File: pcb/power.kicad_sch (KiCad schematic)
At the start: 20 parts, among them U10 NCP163AFCT120T2G, U4 NCP163AFCT330T2G, U5 TPS82695, U9 NCP163AFCT180T2G

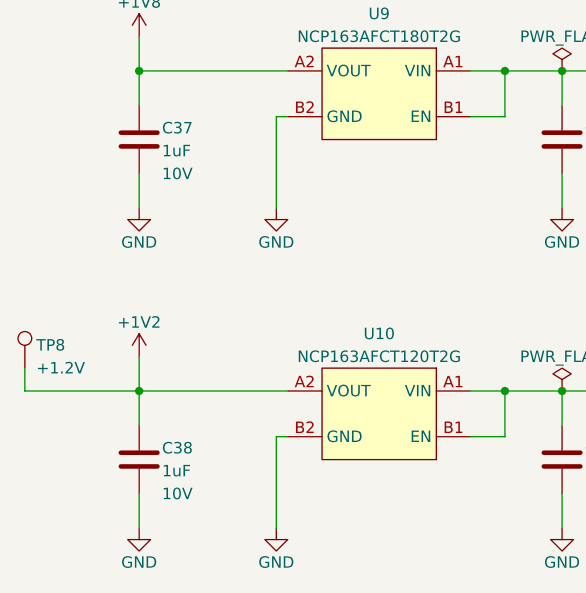
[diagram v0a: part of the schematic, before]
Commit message: Rev. A initial design prior to fab comments
- BOM simplification
- Added my initials to the board
- Made the board more easy to panlize
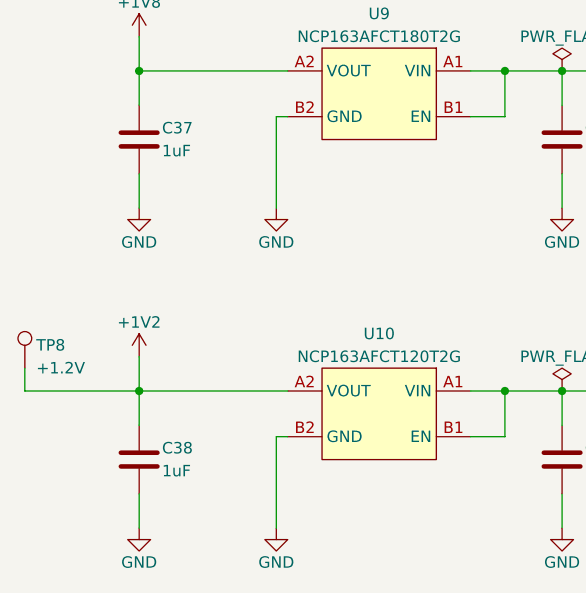
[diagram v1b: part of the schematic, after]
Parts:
- C37, C38: Voltage 10V -> (none)
- TP4, TP8: now left out of the parts list
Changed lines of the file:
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@@
   )
   (symbol (lib_id "Connector:TestPoint") (at 52.07 153.67 0) (unit 1)
-    (in_bom yes) (on_board yes)
+    (in_bom no) (on_board yes)
     (property "Reference" "TP8" (id 0) (at 53.34 151.13 0)
       (effects (font (size 1.27 1.27)) (justify left))
@@
   )
   (symbol (lib_id "Connector:TestPoint") (at 52.07 41.91 0) (unit 1)
-    (in_bom yes) (on_board yes)
+    (in_bom no) (on_board yes)
     (property "Reference" "TP4" (id 0) (at 53.34 39.37 0)
       (effects (font (size 1.27 1.27)) (justify left))
@@
     (property "Datasheet" "~" (id 3) (at 64.77 163.83 0)
       (effects (font (size 1.27 1.27)) hide)
-    )
-    (property "Voltage" "10V" (id 4) (at 67.31 167.64 0)
-      (effects (font (size 1.27 1.27)) (justify left))
     )
     (pin "1")
@@
       (effects (font (size 1.27 1.27)) hide)
     )
-    (property "Voltage" "10V" (id 4) (at 67.31 132.08 0)
-      (effects (font (size 1.27 1.27)) (justify left))
-    )
-    (pin "1")
+    (pin "1")

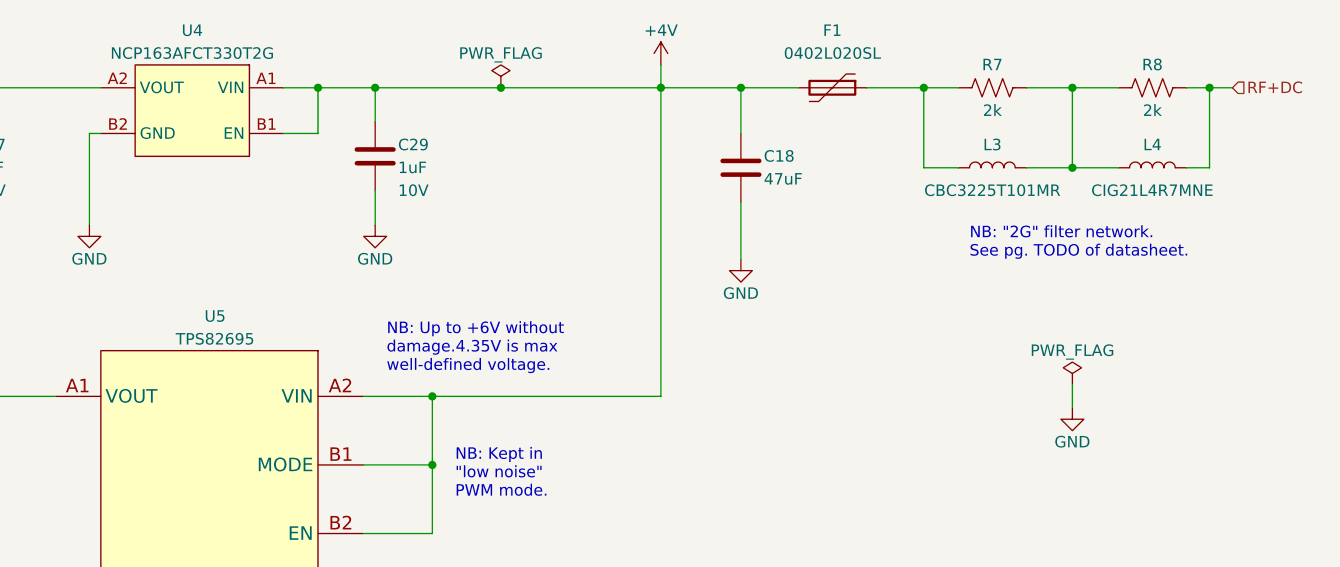
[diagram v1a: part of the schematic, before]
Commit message: Small changes before speedy fabrication
- This is revision A
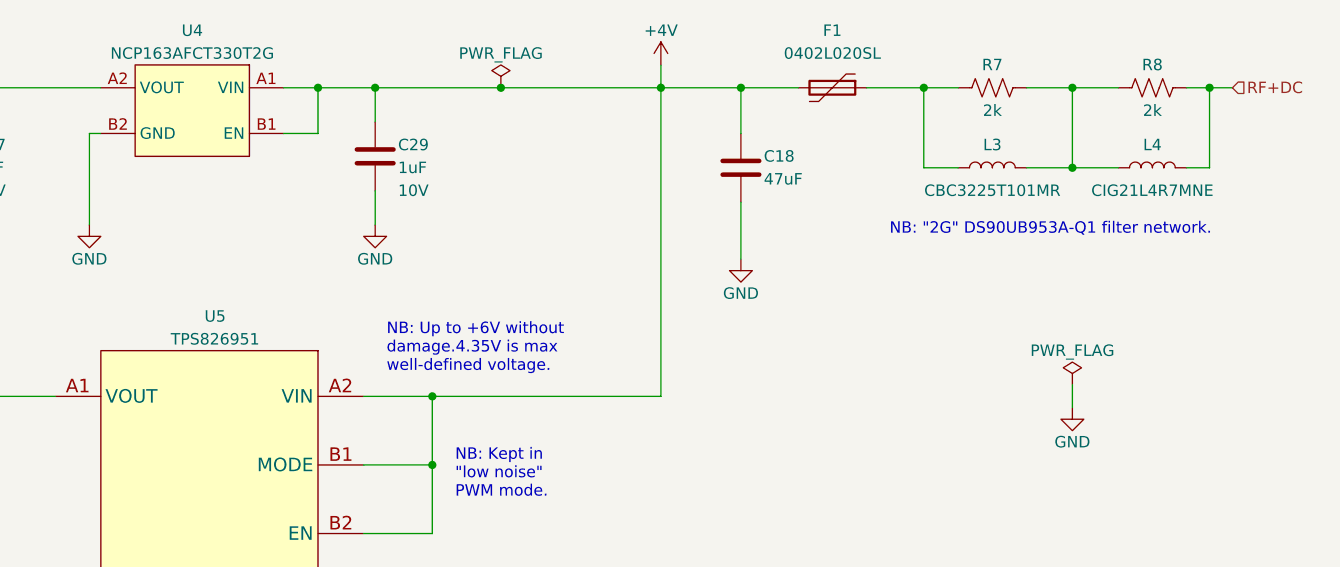
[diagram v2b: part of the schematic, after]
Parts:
- U5: value TPS82695 -> TPS826951
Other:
- note added: "NB: "2G" DS90UB953A-Q1 filter network."
- note removed: "NB: "2G" filter network. See pg. TODO of datasheet."
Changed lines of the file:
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@@
     (effects (font (size 1.27 1.27)) (justify left bottom))
   )
-  (text "NB: \"2G\" filter network.\nSee pg. TODO of datasheet."
-    (at 177.8 63.5 0)
+  (text "NB: \"2G\" DS90UB953A-Q1 filter network." (at 168.91 60.96 0)
     (effects (font (size 1.27 1.27)) (justify left bottom))
   )
@@
     (in_bom yes) (on_board yes)
     (property "Reference" "U5" (id 0) (at 93.98 69.85 0))
-    (property "Value" "TPS82695" (id 1) (at 93.98 72.39 0))
+    (property "Value" "TPS826951" (id 1) (at 93.98 72.39 0))
     (property "Footprint" "jonnew:TI_SIP0008B" (id 2) (at 93.98 109.22 0)
       (effects (font (size 1.27 1.27)) hide)

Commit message: Start of revision B
- Address the following issues
1. The photodiode anode is on pin 3, not pin 2
2. No paste on coax connector
3. CRESET_B needs to come out to programming header
4. Need PU on CS line.
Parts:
- C18, C37, C38: TempCo (none) -> X5R; Voltage (none) -> 10V
- C27, C29, C40, C41: TempCo (none) -> X5R
- TP4, TP8: DNP (none) -> DNP
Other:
- title: Headstage-RHS2116 -> Headstage-64s
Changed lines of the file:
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@@
   (paper "A4")
   (title_block
-    (title "Headstage-RHS2116")
+    (title "Headstage-64s")
     (date "2021-12-16")
-    (rev "A")
+    (rev "B")
     (company "Open Ephys, Inc")
     (comment 1 "Jonathan P. Newman")
@@
       (effects (font (size 1.27 1.27)) hide)
     )
+    (property "DNP" "DNP" (id 4) (at 52.07 153.67 0)
+      (effects (font (size 1.27 1.27)) hide)
+    )
     (pin "1")
   )
@@
       (effects (font (size 1.27 1.27)) hide)
     )
+    (property "DNP" "DNP" (id 4) (at 52.07 41.91 0)
+      (effects (font (size 1.27 1.27)) hide)
+    )
     (pin "1")
   )
@@
       (effects (font (size 1.27 1.27)) (justify left))
     )
+    (property "TempCo" "X5R" (id 5) (at 111.76 52.07 0)
+      (effects (font (size 1.27 1.27)) hide)
+    )
     (pin "1")
     (pin "2")
@@
     )
     (property "Datasheet" "~" (id 3) (at 64.77 163.83 0)
+      (effects (font (size 1.27 1.27)) hide)
+    )
+    (property "TempCo" "X5R" (id 4) (at 64.77 163.83 0)
+      (effects (font (size 1.27 1.27)) hide)
+    )
+    (property "Voltage" "10V" (id 5) (at 64.77 163.83 0)
       (effects (font (size 1.27 1.27)) hide)
     )
@@
     )
     (property "Datasheet" "~" (id 3) (at 152.4 53.34 0)
+      (effects (font (size 1.27 1.27)) hide)
+    )
+    (property "TempCo" "X5R" (id 4) (at 152.4 53.34 0)
+      (effects (font (size 1.27 1.27)) hide)
+    )
+    (property "Voltage" "10V" (id 5) (at 152.4 53.34 0)
       (effects (font (size 1.27 1.27)) hide)
     )
@@
       (effects (font (size 1.27 1.27)) hide)
     )
-    (property "Datasheet" "" (id 3) (at 91.44 46.99 0)
+    (property "Datasheet" "~" (id 3) (at 91.44 46.99 0)
       (effects (font (size 1.27 1.27)) hide)
     )
@@
     (property "Voltage" "10V" (id 4) (at 114.3 167.64 0)
       (effects (font (size 1.27 1.27)) (justify left))
+    )
+    (property "TempCo" "X5R" (id 5) (at 111.76 163.83 0)
+      (effects (font (size 1.27 1.27)) hide)
     )
     (pin "1")
@@
       (effects (font (size 1.27 1.27)) (justify left))
     )
+    (property "TempCo" "X5R" (id 5) (at 111.76 128.27 0)
+      (effects (font (size 1.27 1.27)) hide)
+    )
     (pin "1")
     (pin "2")
@@
       (effects (font (size 1.27 1.27)) (justify left))
     )
+    (property "TempCo" "X5R" (id 5) (at 64.77 52.07 0)
+      (effects (font (size 1.27 1.27)) hide)
+    )
     (pin "1")
     (pin "2")
@@
       (effects (font (size 1.27 1.27)) hide)
     )
+    (property "TempCo" "X5R" (id 4) (at 64.77 128.27 0)
+      (effects (font (size 1.27 1.27)) hide)
+    )
+    (property "Voltage" "10V" (id 5) (at 64.77 128.27 0)
+      (effects (font (size 1.27 1.27)) hide)
+    )
     (pin "1")
     (pin "2")
@@
       (effects (font (size 1.27 1.27)) hide)
     )
-    (property "Datasheet" "" (id 3) (at 91.44 158.75 0)
+    (property "Datasheet" "~" (id 3) (at 91.44 158.75 0)
       (effects (font (size 1.27 1.27)) hide)
     )
@@
       (effects (font (size 1.27 1.27)) hide)
     )
-    (property "Datasheet" "" (id 3) (at 184.15 48.26 0)
+    (property "Datasheet" "~" (id 3) (at 184.15 48.26 0)
       (effects (font (size 1.27 1.27)) hide)
     )
@@
       (effects (font (size 1.27 1.27)) hide)
     )
-    (property "Datasheet" "" (id 3) (at 91.44 123.19 0)
-      (effects (font (size 1.27 1.27)) hide)
-    )
+    (property "Datasheet" "~" (id 3) (at 91.44 123.19 0)
+      (effects (font (size 1.27 1.27)) hide)
+    )
